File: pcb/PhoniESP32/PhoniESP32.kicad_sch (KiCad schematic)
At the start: 24 parts, among them J3 Conn_Buttons, U3 ESP32-C6-MINI-1U-H4

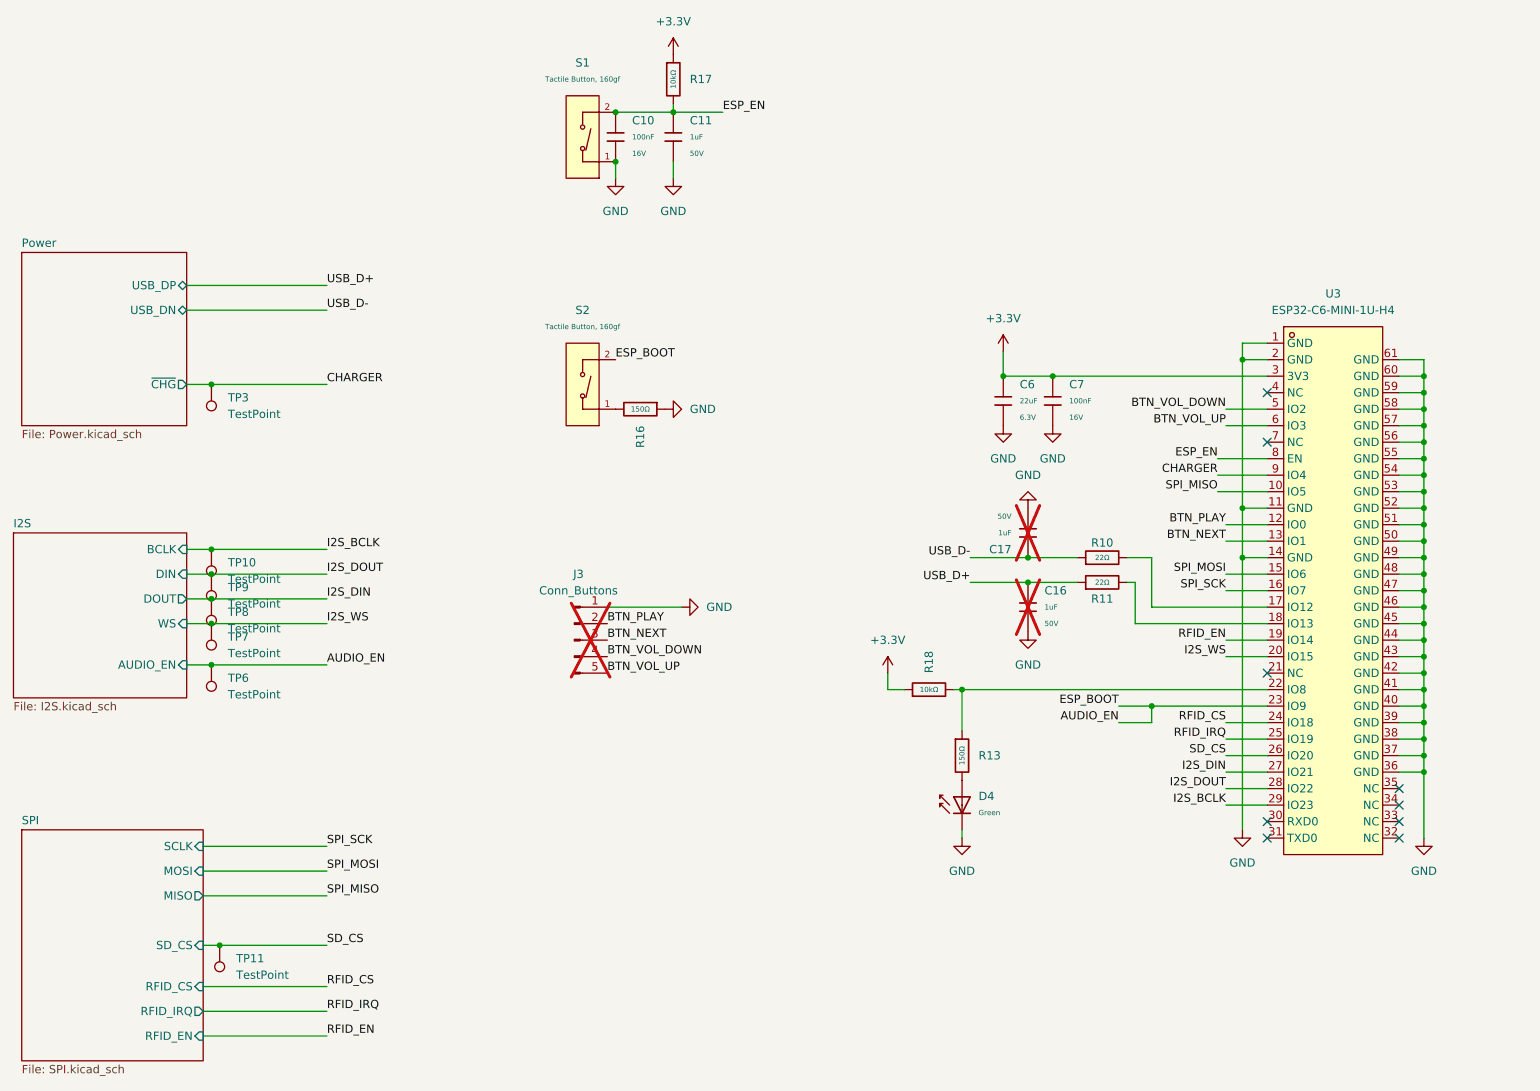
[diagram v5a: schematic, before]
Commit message: feat(pcb): version for hand soldering
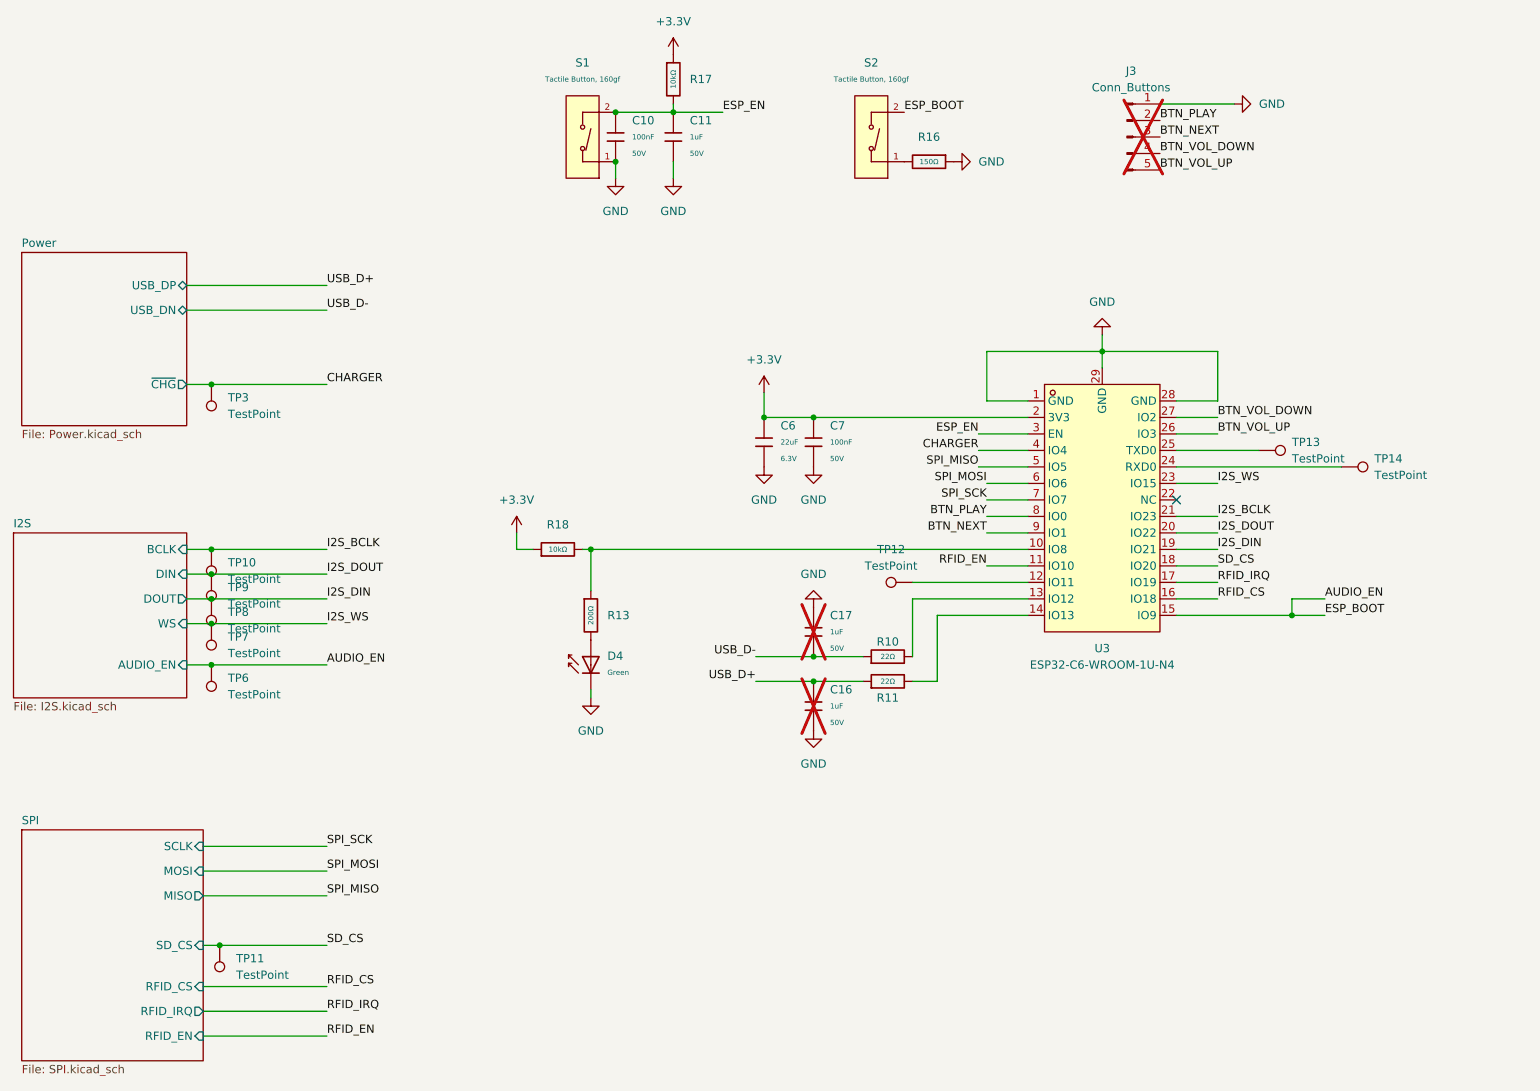
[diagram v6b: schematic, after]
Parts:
- removed R13: 150Ω, PCM_JLCPCB:R_0603, symbol PCM_JLCPCB-Resistors:0603,150Ω
- removed U3: ESP32-C6-MINI-1U-H4, JLCPCB:WIFIM-SMD_61P-L13.2-W12.5-P0.80, symbol JLCPCB:ESP32-C6-MINI-1U-H4
- added R13: 200Ω, PCM_JLCPCB:R_0603, symbol PCM_JLCPCB-Resistors:0603,200Ω
- added TP12, TP13, TP14: TestPoint, TestPoint:TestPoint_Pad_D1.0mm, symbol Connector:TestPoint
- added U3: ESP32-C6-WROOM-1U-N4, JLCPCB:WIFIM-SMD_28P-L19.2-W18.0-P1.27-TL, symbol JLCPCB:ESP32-C6-WROOM-1U-N4
- C10, C7: footprint PCM_JLCPCB:C_0402 -> PCM_JLCPCB:C_0603; symbol PCM_JLCPCB-Capacitors:0402,100nF -> PCM_JLCPCB-Capacitors:0603,100nF; LCSC C1525 -> C14663; Manufacturer Samsung Electro-Mechanics -> YAGEO; Part CL05B104KO5NNNC -> CC0603KRX7R9BB104; Price 0.004USD -> 0.006USD; Stock 20208285 -> 70324515; Voltage Rated 16V -> 50V
- C16, C17: now in the parts list
- D4: MPN (none) -> KT-0805G
- J3: LCSC Part (none) -> C225480; MPN (none) -> A2541WV-5P
- R10, R11: footprint PCM_JLCPCB:R_0402 -> PCM_JLCPCB:R_0603; symbol PCM_JLCPCB-Resistors:0402,22Ω -> PCM_JLCPCB-Resistors:0603,22Ω; LCSC C25092 -> C23345; Overload Voltage (Max) 50V -> 75V; Part 0402WGF220JTCE -> 0603WAF220JT5E; Power(Watts) 62.5mW -> 100mW; Stock 7466061 -> 4414856
- S1, S2: MPN (none) -> TS-1088-AR02016
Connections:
- net +3.3V: now also U3.2 (3V3)
- net AUDIO_EN: now also U3.15 (IO9)
- net BTN_NEXT: now also U3.9 (IO1)
- net BTN_PLAY: now also U3.8 (IO0)
- net BTN_VOL_DOWN: now also U3.27 (IO2)
- net BTN_VOL_UP: now also U3.26 (IO3)
- net CHARGER: now also U3.4 (IO4)
- net ESP_EN: now also U3.3 (EN)
- net GND: now also U3.1 (GND), U3.28 (GND), U3.29 (GND)
- net I2S_BCLK: now also U3.21 (IO23)
- net I2S_DIN: now also U3.19 (IO21)
- net I2S_DOUT: now also U3.20 (IO22)
- net I2S_WS: now also U3.23 (IO15)
- net RFID_CS: now also U3.16 (IO18)
- net RFID_EN: now also U3.11 (IO10)
- net RFID_IRQ: now also U3.17 (IO19)
- net SD_CS: now also U3.18 (IO20)
- net SPI_MISO: now also U3.5 (IO5)
- net SPI_MOSI: now also U3.6 (IO6)
- net SPI_SCK: now also U3.7 (IO7)
- net at D4.2: now also R13.2
- net at R10.2: now also U3.13 (IO12)
- net at R11.2: now also U3.14 (IO13)
- net at R18.2: now also R13.1, U3.10 (IO8)
- new net: TP12.1, U3.12 (IO11)
- new net: TP14.1, U3.24 (RXD0)
- new net: TP13.1, U3.25 (TXD0)
- no-connect marks 9 -> 1
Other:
- title: (none) -> PhoniESP32
- moved on the sheet: C16, C17, C6, C7, D4, J3, R10, R11, R16, R18, S2
